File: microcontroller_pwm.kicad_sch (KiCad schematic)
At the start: 2 parts, among them U1 6N135, U2 6N135

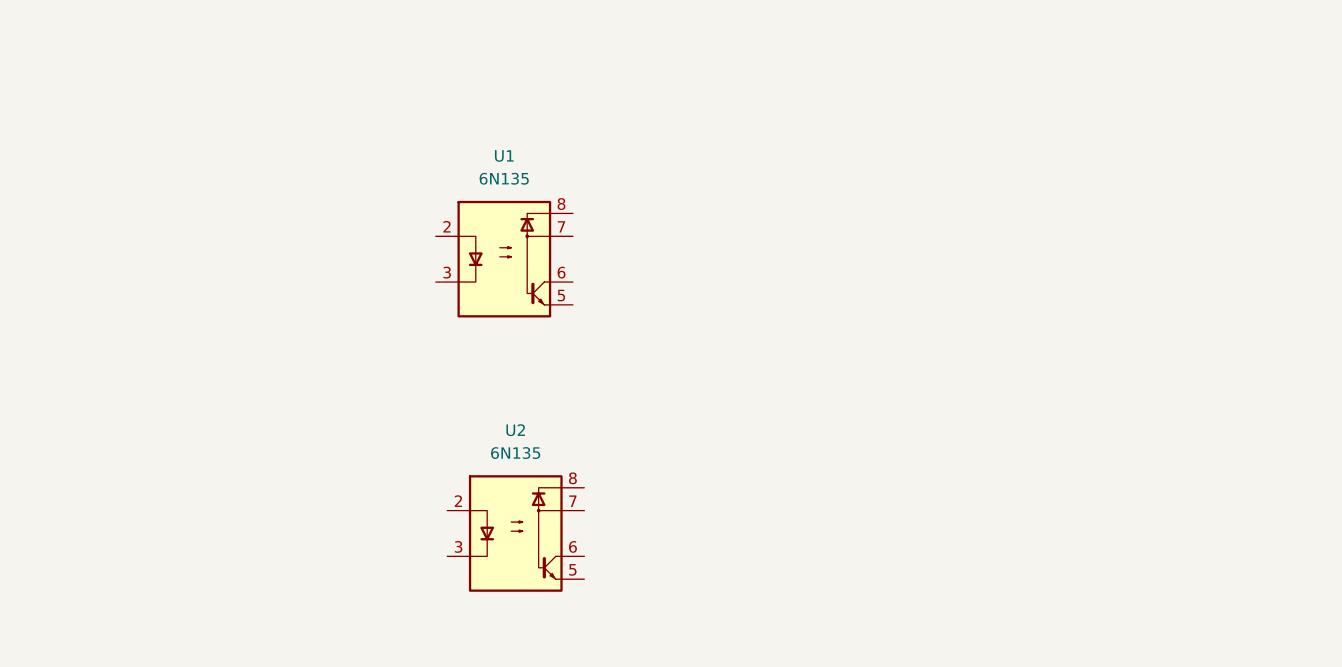
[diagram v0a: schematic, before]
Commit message: Done upto shunt circuit, H-bridge, remaining Loogic
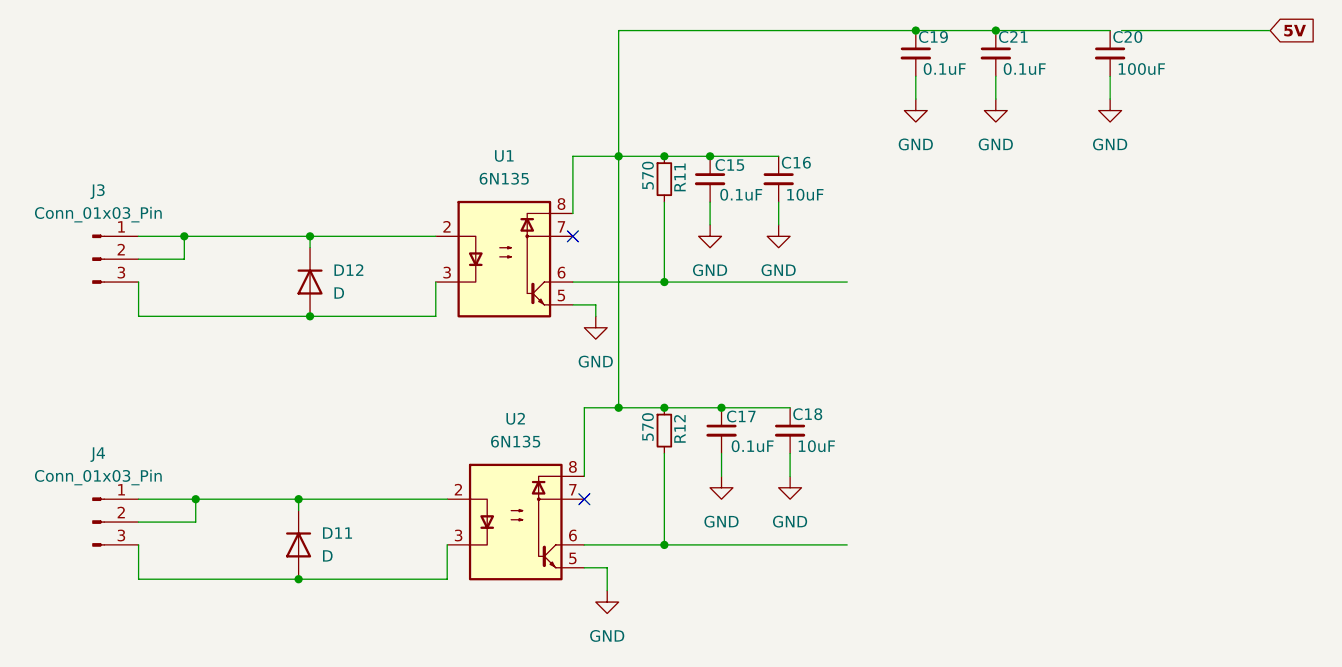
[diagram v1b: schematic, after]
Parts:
- added C15, C17, C19, C21: 0.1uF, symbol Device:C_Small
- added C16, C18: 10uF, symbol Device:C_Small
- added C20: 100uF, symbol Device:C_Small
- added D11, D12: D, symbol Device:D
- added J3, J4: Conn_01x03_Pin, symbol Connector:Conn_01x03_Pin
- added R11, R12: 570, symbol Device:R_Small
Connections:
- net at U2.2: now also D11.1 (K), J4.1 (Pin_1), J4.2 (Pin_2)
- net at U2.3: now also D11.2 (A), J4.3 (Pin_3)
- net GND: now reaches U2.5
- net GND: now also U1.5, C15.2, C16.2, C17.2, C18.2, C19.2, C20.2, C21.2
- net at U2.6: now also R12.2
- net at U2.8: now also U1.8, C15.1, C16.1, C17.1, C18.1, C19.1, C20.1, C21.1, R11.1, R12.1
- net at U1.2: now also D12.1 (K), J3.1 (Pin_1), J3.2 (Pin_2)
- net at U1.3: now also D12.2 (A), J3.3 (Pin_3)
- net at U1.6: now also R11.2
- no-connect marks 0 -> 2
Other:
- moved on the sheet: U2
